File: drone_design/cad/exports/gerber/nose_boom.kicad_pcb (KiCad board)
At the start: 2 copper layers, 380 x 20 mm, 0 parts

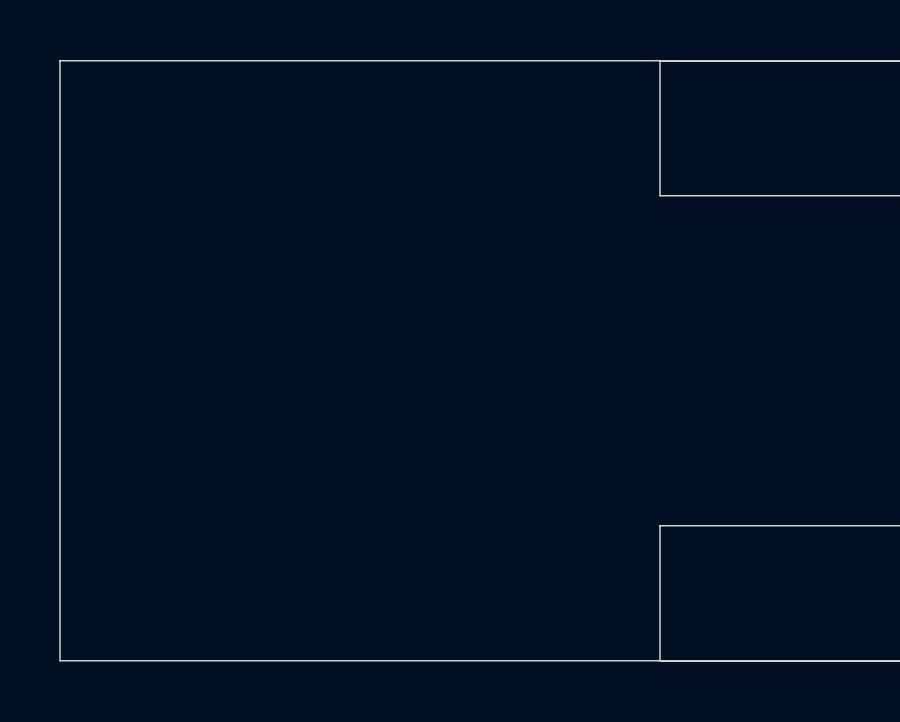
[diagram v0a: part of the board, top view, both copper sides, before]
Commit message: feat: fix ToF bracket alignment, add motor mount to arm tips
- Fix all 6 ToF sensor/bracket positions with correct rotations
  so sensors sit flush against bracket tab faces, sensing outward
- Add circular motor mounting plate at arm tips (25mm dia)
  with 4x M2 bolt holes on 16mm circle + center shaft clearance
- Add matching M2 threaded holes to motor base plate model
- Rebuild all STLs and viewer (68 parts, 15.8 MB total)
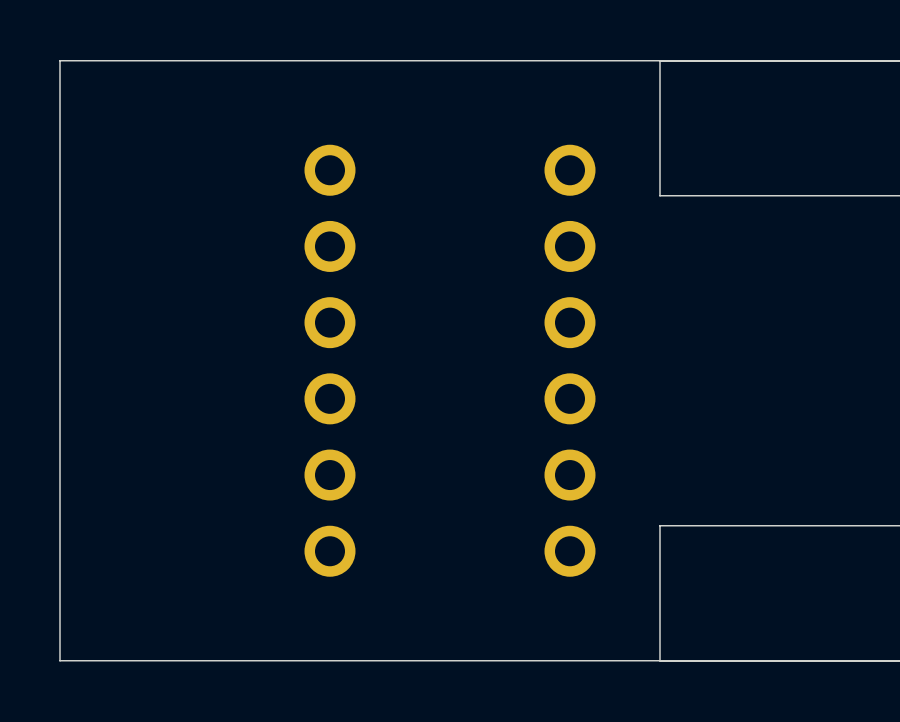
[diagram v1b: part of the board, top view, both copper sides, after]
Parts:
- added ?: , MountingHole:MountingHole_1.0mm, F.Cu at (-181.0, -6.35)
- added ?: , MountingHole:MountingHole_1.0mm, F.Cu at (-173.0, 1.27)
- added ?: , MountingHole:MountingHole_1.0mm, F.Cu at (-173.0, 3.81)
- added ?: , MountingHole:MountingHole_1.0mm, F.Cu at (-173.0, 6.35)
- added ?: , MountingHole:MountingHole_1.0mm, F.Cu at (-181.0, -3.81)
- added ?: , MountingHole:MountingHole_1.0mm, F.Cu at (-181.0, -1.27)
- added ?: , MountingHole:MountingHole_1.0mm, F.Cu at (-181.0, 1.27)
- added ?: , MountingHole:MountingHole_1.0mm, F.Cu at (-181.0, 3.81)
- added ?: , MountingHole:MountingHole_1.0mm, F.Cu at (-181.0, 6.35)
- added ?: , MountingHole:MountingHole_1.0mm, F.Cu at (-173.0, -6.35)
- added ?: , MountingHole:MountingHole_1.0mm, F.Cu at (-173.0, -3.81)
- added ?: , MountingHole:MountingHole_1.0mm, F.Cu at (-173.0, -1.27)
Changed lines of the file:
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@@
   (gr_line (start 170.0000 10.0000) (end -170.0000 10.0000) (layer "Edge.Cuts") (width 0.05))
   (gr_line (start -170.0000 10.0000) (end -170.0000 5.5000) (layer "Edge.Cuts") (width 0.05))
+  (footprint "MountingHole:MountingHole_1.0mm" (layer "F.Cu")
+    (at -181.0000 -6.3500)
+    (pad "" thru_hole circle (at 0 0) (size 1.70 1.70) (drill 1.00)
+      (layers "*.Cu" "*.Mask")
+    )
+  )
+  (footprint "MountingHole:MountingHole_1.0mm" (layer "F.Cu")
+    (at -181.0000 -3.8100)
+    (pad "" thru_hole circle (at 0 0) (size 1.70 1.70) (drill 1.00)
+      (layers "*.Cu" "*.Mask")
+    )
+  )
+  (footprint "MountingHole:MountingHole_1.0mm" (layer "F.Cu")
+    (at -181.0000 -1.2700)
+    (pad "" thru_hole circle (at 0 0) (size 1.70 1.70) (drill 1.00)
+      (layers "*.Cu" "*.Mask")
+    )
+  )
+  (footprint "MountingHole:MountingHole_1.0mm" (layer "F.Cu")
+    (at -181.0000 1.2700)
+    (pad "" thru_hole circle (at 0 0) (size 1.70 1.70) (drill 1.00)
+      (layers "*.Cu" "*.Mask")
+    )
+  )
+  (footprint "MountingHole:MountingHole_1.0mm" (layer "F.Cu")
+    (at -181.0000 3.8100)
+    (pad "" thru_hole circle (at 0 0) (size 1.70 1.70) (drill 1.00)
+      (layers "*.Cu" "*.Mask")
+    )
+  )
+  (footprint "MountingHole:MountingHole_1.0mm" (layer "F.Cu")
+    (at -181.0000 6.3500)
+    (pad "" thru_hole circle (at 0 0) (size 1.70 1.70) (drill 1.00)
+      (layers "*.Cu" "*.Mask")
+    )
+  )
+  (footprint "MountingHole:MountingHole_1.0mm" (layer "F.Cu")
+    (at -173.0000 -6.3500)
+    (pad "" thru_hole circle (at 0 0) (size 1.70 1.70) (drill 1.00)
+      (layers "*.Cu" "*.Mask")
+    )
+  )
+  (footprint "MountingHole:MountingHole_1.0mm" (layer "F.Cu")
+    (at -173.0000 -3.8100)
+    (pad "" thru_hole circle (at 0 0) (size 1.70 1.70) (drill 1.00)
+      (layers "*.Cu" "*.Mask")
+    )
+  )
+  (footprint "MountingHole:MountingHole_1.0mm" (layer "F.Cu")
+    (at -173.0000 -1.2700)
+    (pad "" thru_hole circle (at 0 0) (size 1.70 1.70) (drill 1.00)
+      (layers "*.Cu" "*.Mask")
+    )
+  )
+  (footprint "MountingHole:MountingHole_1.0mm" (layer "F.Cu")
+    (at -173.0000 1.2700)
+    (pad "" thru_hole circle (at 0 0) (size 1.70 1.70) (drill 1.00)
+      (layers "*.Cu" "*.Mask")
+    )
+  )
+  (footprint "MountingHole:MountingHole_1.0mm" (layer "F.Cu")
+    (at -173.0000 3.8100)
+    (pad "" thru_hole circle (at 0 0) (size 1.70 1.70) (drill 1.00)
+      (layers "*.Cu" "*.Mask")
+    )
+  )
+  (footprint "MountingHole:MountingHole_1.0mm" (layer "F.Cu")
+    (at -173.0000 6.3500)
+    (pad "" thru_hole circle (at 0 0) (size 1.70 1.70) (drill 1.00)
+      (layers "*.Cu" "*.Mask")
+    )
+  )
   (gr_text "BOOM" (at 0.0000 0.0000) (layer "F.SilkS")
     (effects (font (size 2 2) (thickness 0.2)))
